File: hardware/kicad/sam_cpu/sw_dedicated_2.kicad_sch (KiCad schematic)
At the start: 46 parts, among them J13 J13 DEDICATED, SW3 DIP x8, U14 74HC165, U15 74HC165

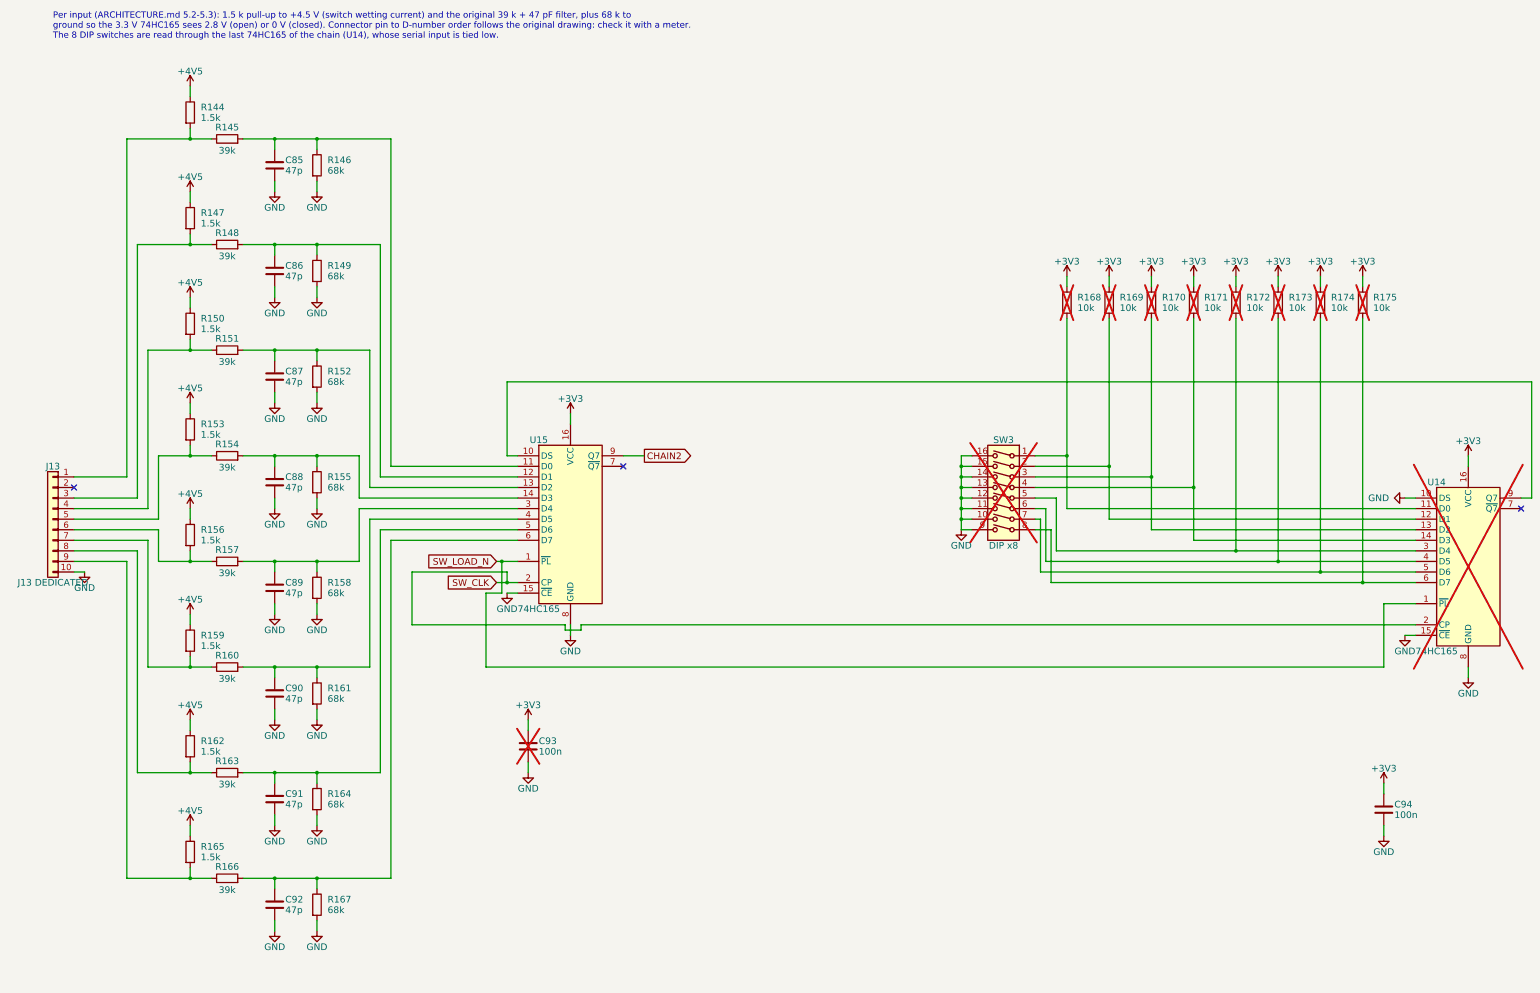
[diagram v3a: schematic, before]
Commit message: Remove USB-C, GI dimmer, SWD header and DIP block; Pi SWD on GPIO24/25 as raspberrypi-swd.cfg
c35 (schematic) and c36 (board): J19 with R10-R14, the GI dimmer sheet (J18, R183-R185),
J20, and the DIP block (SW3, R168-R175, C93, U14) go to free routing space. U15's serial
input goes to GND. J21 pin 18 (GPIO24) is now SWDIO and pin 22 (GPIO25) SWCLK, matching
Raspberry Pi's OpenOCD interface/raspberrypi-swd.cfg. ERC clean, schematic parity clean.

Co-Authored-By: Claude Opus 5.5 (1M context) <noreply@anthropic.com>
Claude-Session: https://claude.ai/code/session_01QQate2kninVTv93dgZ4pfZ
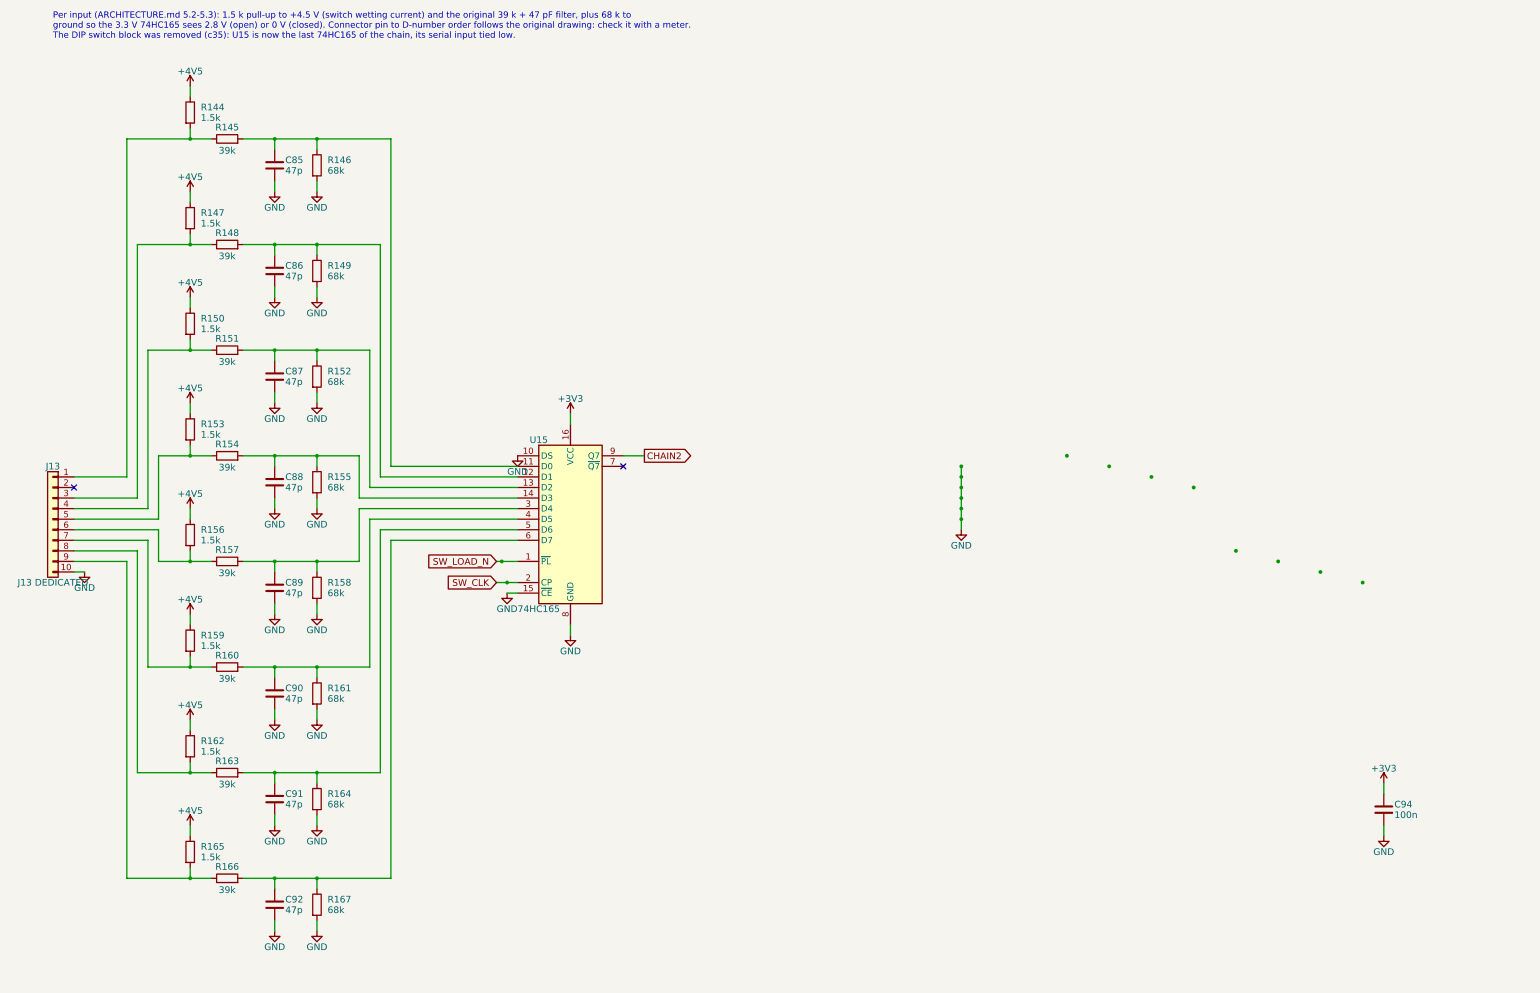
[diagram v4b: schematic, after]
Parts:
- removed C93: 100n, Capacitor_SMD:C_0603_1608Metric, symbol Device:C
- removed R168, R169, R170, R171, R172, R173, R174, R175: 10k, Resistor_SMD:R_0603_1608Metric, symbol Device:R
- removed SW3: DIP x8, Button_Switch_THT:SW_DIP_SPSTx08_Slide_9.78x22.5mm_W7.62mm_P2.54mm, symbol Switch:SW_DIP_x08
- removed U14: 74HC165, Package_SO:SOIC-16_3.9x9.9mm_P1.27mm, symbol 74xx:74HC165
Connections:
- net GND: now also U15.10 (DS)
- no-connect marks 3 -> 2
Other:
- note added: "Per input (ARCHITECTURE.md 5.2-5.3): 1.5 k pull-up to +4.5 V (switch wetting current) and the original 39 k + 47 pF filter, plus 68 k to ground so the 3.3 V 74HC165 sees 2.8 V (open) or 0 V (closed). Connector pin to D-number order follows the original drawing: check it with a meter. The DIP switch block was removed (c35): U15 is now the last 74HC165 of the chain, its serial input tied low."
- note removed: "Per input (ARCHITECTURE.md 5.2-5.3): 1.5 k pull-up to +4.5 V (switch wetting current) and the original 39 k + 47 pF filter, plus 68 k to ground so the 3.3 V 74HC165 sees 2.8 V (open) or 0 V (closed). Connector pin to D-number order follows the original drawing: check it with a meter. The 8 DIP switches are read through the last 74HC165 of the chain (U14), whose serial input is tied low."
